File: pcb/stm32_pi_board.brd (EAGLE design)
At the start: 84 x 56 mm, 96 parts, among them IC1 MIC5219-3.3, IC2 ESP-11, IC3 IS31AP2005, IC4 STM32F405RG, IC5 STF203-22, IC6 MIC5219-3.3, IC7 IS31AP2005, IC8 MIC5219-3.3, IC9 UDA1334ATS, Q1 FDG6332C, Q5 BSH205, X1 PJ-043-SMT, X2 DM3AT, X3 XM7D-0512

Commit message: New version of pi_board
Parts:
- removed ESPJ2: LSP10, MyComponents:LSP10
- removed IC1: MIC5219-3.3, MyComponents:SOT23-5
- removed SV2: 75867-331LF, MyComponents:MA03-2
- added C38: 0.1uF, MyComponents:C0805
- added GN-RX-TX: (no value), MyComponents:MA03-1
- added IC10: REG1117, MyComponents:SOT223
- added L3: 1 uH, MyComponents:L0805
- added R26, R27: 330, MyComponents:R0805
- added R28: 1, MyComponents:R0805
- C6: value 470pF -> 100 uF; device MyComponents:C0805 -> MyComponents:CPOL1311
- C7: value 2.2uF -> 47 uF
- D1: value WP154A4SUREQBFZGC -> (none); device MyComponents:RGB-LED-5MM -> MyComponents:RGB-LED-SMD-3X1
- FLASH: value LSP10 -> (none); device MyComponents:LSP10 -> MyComponents:MA02-1
- HSE: device MyComponents:Q-FA-128 -> MyComponents:Q-HC-46X
- moved RESET 63.1 mm to (19.0, 30.8), turned to 90 degrees
- moved C16 62.4 mm to (22.5, 33.2), flipped to the bottom, turned to 0 degrees
- moved SV1 61.5 mm to (11.0, 27.0)
- moved D1 41.8 mm to (82.5, 43.5)
- moved R6 40.3 mm to (78.2, 44.2), flipped to the top, turned to 180 degrees
- moved C6 7.85 mm to (27.0, 29.5), flipped to the top, turned to 270 degrees
- moved R3 7.04 mm to (9.00, 40.0), turned to 180 degrees
- moved C15 6.82 mm to (49.0, 41.8), turned to 270 degrees
- moved C14 5.87 mm to (32.2, 28.8), turned to 90 degrees
- moved C2 5.35 mm to (9.00, 42.5)
- moved IC6 5.13 mm to (13.2, 41.2), turned to 0 degrees
- moved R8 4.76 mm to (56.2, 26.6), flipped to the bottom, turned to 180 degrees
- moved R7 4.65 mm to (50.5, 33.8), turned to 0 degrees
- moved C7 4.14 mm to (30.0, 28.8), flipped to the top, turned to 270 degrees
- moved C3 4.12 mm to (13.2, 45.0)
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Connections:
- removed net D1_BLUE: D1.AB, IC4.10
- removed net D1_GREEN: D1.AG, IC4.9
- removed net D1_RED: D1.AR, IC4.11
- new net N$75: D1.P$1, R27.1
- new net N$85: IC10.2, R28.2
- new net N$90: L3.1, R28.1
- new net PC1: IC4.9, SV3.6
- new net PC2: IC4.10, SV3.5
- new net PC3: IC4.11, SV3.4
- net ESP-IO0: now also FLASH.1; no longer FLASH.MP
- net ESP-RXI: now also GN-RX-TX.2; no longer SV2.5
- net ESP-TXI: now also GN-RX-TX.3; no longer SV2.3
- net GND: now also C38.2, C6.2-, D1.P$2, FLASH.2, GN-RX-TX.1, IC10.1; no longer C6.1, ESPJ2.MP, IC1.2, R6.2, SV2.1
- net N$40: now also D1.P$4, R26.1; no longer D1.C, R6.1
- net N$5: now also D1.P$3, R6.1; no longer C6.2, IC1.4
- net N$78: now also HSE.2; no longer HSE.3
- net PB4: now also R27.2; no longer SV3.11
- net PB5: now also R26.2; no longer SV3.10
- net PB6: now also SV3.11; no longer SV3.9
- net PB7: now also SV3.10; no longer SV3.8
- net PB8: now also R6.2; no longer SV3.7
- net PB9: now also SV3.9; no longer SV3.6
- net PC0: now also SV3.7; no longer SV3.4
- net PC13: now also SV3.8; no longer SV3.5
- net VDD: now also C6.1+, L3.2; no longer IC1.5
- net VIN: now also C38.1, IC10.3; no longer IC1.1, IC1.3
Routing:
- net VDD: track 146.9 -> 118.7 mm, vias 6 -> 8
- net SWCLK: track 22.2 -> 50.0 mm, vias 0 -> 2
- net PC1: track 0.00 -> 25.6 mm
- net PC2: track 0.00 -> 24.8 mm
- net PC3: track 0.00 -> 23.9 mm
- net D1_GREEN: track 18.9 -> 0.00 mm
- net D1_BLUE: track 17.0 -> 0.00 mm
- net ESP-IO0: track 38.3 -> 22.4 mm
- net SWDIO: track 36.6 -> 50.5 mm, vias 0 -> 2
- net D1_RED: track 13.7 -> 0.00 mm
- net ESP-TXI: track 25.8 -> 13.8 mm
- net PC13: track 38.1 -> 26.9 mm
- net GND: track 101.3 -> 90.6 mm, vias 19 -> 21
- net ESP-ON1: track 45.0 -> 36.2 mm
- net ESP-RXI: track 23.3 -> 14.5 mm
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- added copper zone on layer 1, net VDD
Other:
- board text added: "PC1"
- board text added: "PC2"
- board text added: "PC3"
- board text added: "VCC/"
- board text added: "x3"
- board text removed: "PB4"
- board text removed: "PB5"
- board text removed: "PB8"
- board text removed: "RX"
- board text removed: "TX"
- board text removed: "VCC"

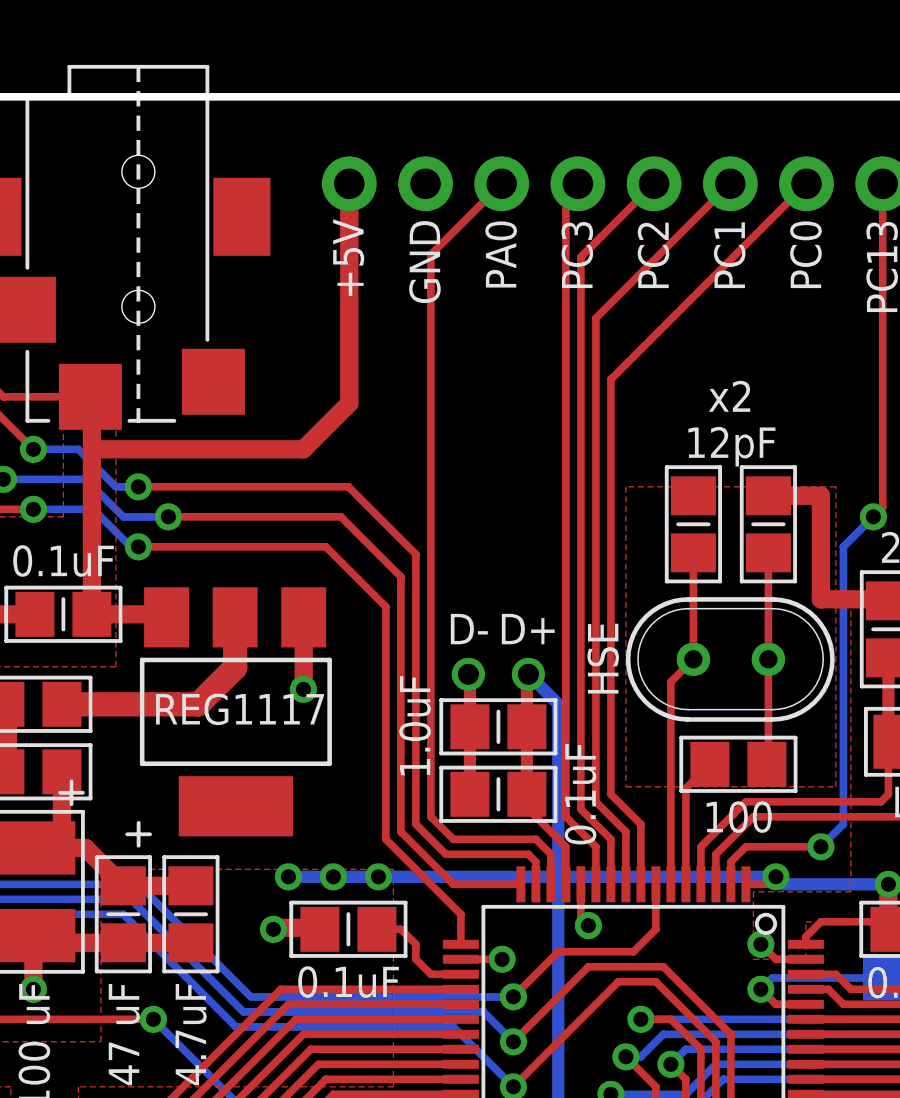
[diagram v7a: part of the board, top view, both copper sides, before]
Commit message: Added LMT86
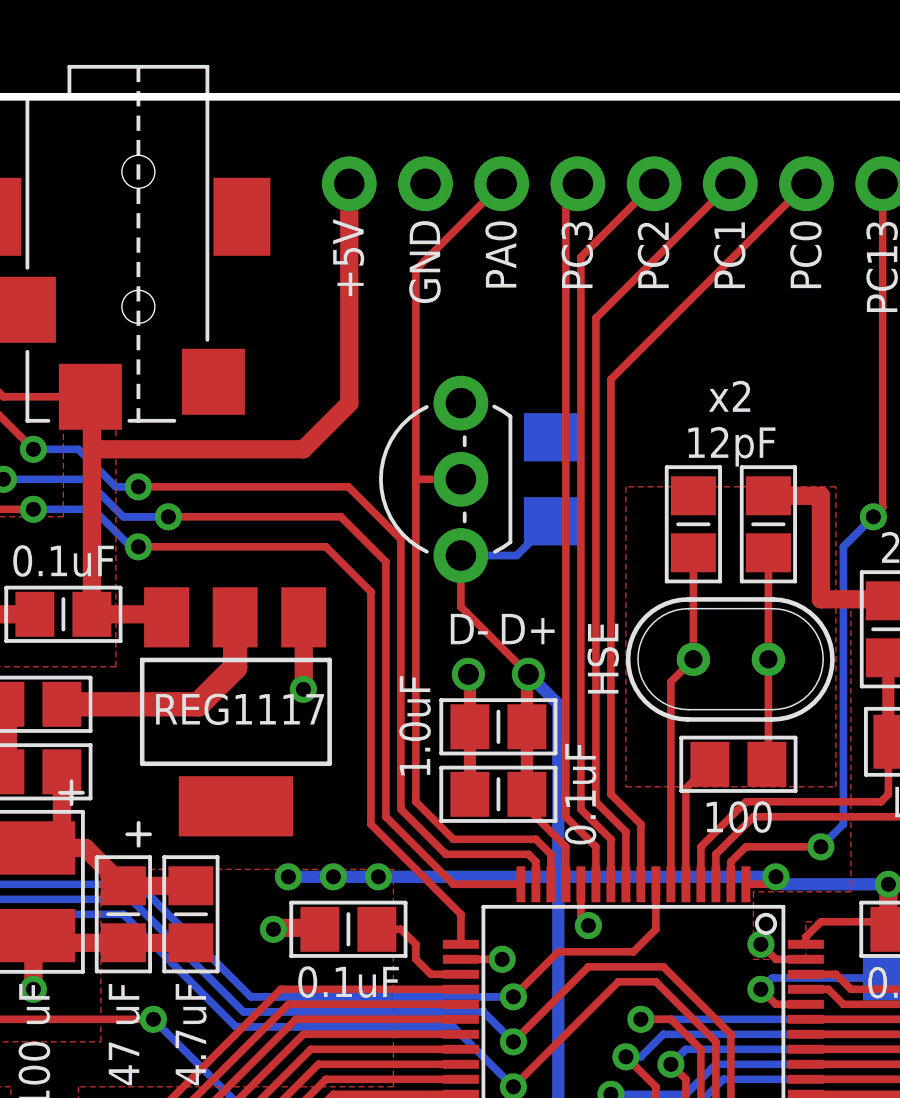
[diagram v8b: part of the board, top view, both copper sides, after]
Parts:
- added C39: 0.1 uF, rcl:C1206
- added IC1: LMT86, MyComponents:LMT86
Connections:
- net GND: now also C39.1, IC1.GND
- net PA0: now also IC1.OUT
- net VDD: now also C39.2, IC1.VDD
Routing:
- net VDD: track 118.7 -> 127.1 mm
- net PA0: track 27.6 -> 29.5 mm
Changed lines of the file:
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@@
 <layer number="21" name="tPlace" color="7" fill="1" visible="yes" active="yes"/>
 <layer number="22" name="bPlace" color="7" fill="1" visible="yes" active="yes"/>
-<layer number="23" name="tOrigins" color="15" fill="1" visible="no" active="yes"/>
+<layer number="23" name="tOrigins" color="15" fill="1" visible="yes" active="yes"/>
 <layer number="24" name="bOrigins" color="15" fill="1" visible="yes" active="yes"/>
-<layer number="25" name="tNames" color="7" fill="1" visible="no" active="yes"/>
+<layer number="25" name="tNames" color="7" fill="1" visible="yes" active="yes"/>
 <layer number="26" name="bNames" color="7" fill="1" visible="yes" active="yes"/>
-<layer number="27" name="tValues" color="7" fill="1" visible="no" active="yes"/>
-<layer number="28" name="bValues" color="7" fill="1" visible="no" active="yes"/>
+<layer number="27" name="tValues" color="7" fill="1" visible="yes" active="yes"/>
+<layer number="28" name="bValues" color="7" fill="1" visible="yes" active="yes"/>
 <layer number="29" name="tStop" color="7" fill="3" visible="no" active="yes"/>
 <layer number="30" name="bStop" color="7" fill="6" visible="no" active="yes"/>
@@
 <attribute name="VALUE" x="24.75" y="35.73" size="1.016" layer="25" rot="R180" align="center-left"/>
 </element>
+<element name="IC1" library="MyComponents" package="LMT86" value="LMT86" x="41.25" y="43.25" locked="yes" smashed="yes" rot="R90">
+<attribute name="VALUE" x="43.25" y="43.25" size="1.016" layer="27" ratio="10" rot="R270" align="bottom-center"/>
+</element>
+<element name="C39" library="rcl" package="C1206" value="0.1 uF" x="44.25" y="43.25" locked="yes" smashed="yes" rot="MR270">
+<attribute name="VALUE" x="45.774" y="43.25" size="1.016" layer="26" rot="MR90" align="bottom-center"/>
+</element>
 </elements>
 <signals>
@@
 <wire x1="36.0106" y1="36.2606" x2="36" y2="36.25" width="0.6096" layer="1"/>
 <wire x1="27" y1="28.038" x2="27" y2="26.25" width="0.6096" layer="1"/>
+<contactref element="IC1" pad="GND"/>
+<contactref element="C39" pad="1"/>
 </signal>
 <signal name="VIN">
@@
 <wire x1="44.75" y1="31" x2="43.45" y2="32.3" width="0.254" layer="1"/>
 <wire x1="43.45" y1="32.3" x2="43.45" y2="32.75" width="0.254" layer="1"/>
+<contactref element="IC1" pad="VDD"/>
+<contactref element="C39" pad="2"/>
+<wire x1="41.25" y1="40.71" x2="41.25" y2="39" width="0.254" layer="1"/>
+<wire x1="41.25" y1="39" x2="43.5" y2="36.75" width="0.254" layer="1"/>
+<wire x1="41.25" y1="40.71" x2="43.11" y2="40.71" width="0.254" layer="16"/>
+<wire x1="43.11" y1="40.71" x2="44.25" y2="41.85" width="0.254" layer="16"/>
 </signal>
 <signal name="NRST">
@@
 <wire x1="43.75" y1="31.25" x2="41" y2="31.25" width="0.254" layer="1"/>
 <contactref element="SV3" pad="3"/>
-<wire x1="40.25" y1="50.74" x2="42.61" y2="53.1" width="0.254" layer="1"/>
-<wire x1="41" y1="31.25" x2="40.25" y2="32" width="0.254" layer="1"/>
-<wire x1="40.25" y1="32" x2="40.25" y2="50.74" width="0.254" layer="1"/>
+<wire x1="39.75" y1="50.24" x2="42.61" y2="53.1" width="0.254" layer="1"/>
+<wire x1="41" y1="31.25" x2="39.75" y2="32.5" width="0.254" layer="1"/>
+<wire x1="39.75" y1="32.5" x2="39.75" y2="43.25" width="0.254" layer="1"/>
+<contactref element="IC1" pad="OUT"/>
+<wire x1="39.75" y1="43.25" x2="39.75" y2="50.24" width="0.254" layer="1"/>
+<wire x1="41.25" y1="43.25" x2="39.75" y2="43.25" width="0.254" layer="1"/>
 </signal>
 <signal name="ESP-TX">
@@
 <wire x1="43.25" y1="29.75" x2="41" y2="29.75" width="0.254" layer="1"/>
 <wire x1="23.5" y1="45.75" x2="26" y2="43.25" width="0.254" layer="1"/>
-<wire x1="39.25" y1="40" x2="39.25" y2="31.5" width="0.254" layer="1"/>
-<wire x1="41" y1="29.75" x2="39.25" y2="31.5" width="0.254" layer="1"/>
+<wire x1="38.75" y1="40.5" x2="38.75" y2="32" width="0.254" layer="1"/>
+<wire x1="41" y1="29.75" x2="38.75" y2="32" width="0.254" layer="1"/>
 <wire x1="31.5" y1="42" x2="37.25" y2="42" width="0.254" layer="1"/>
-<wire x1="37.25" y1="42" x2="39.25" y2="40" width="0.254" layer="1"/>
+<wire x1="37.25" y1="42" x2="38.75" y2="40.5" width="0.254" layer="1"/>
 <wire x1="23.1" y1="45.75" x2="23.5" y2="45.75" width="0.254" layer="1"/>
 <wire x1="31.5" y1="42" x2="30" y2="42" width="0.254" layer="16"/>
@@
 <wire x1="41.25" y1="27.75" x2="41.25" y2="28.75" width="0.254" layer="1"/>
 <wire x1="23.1" y1="43.25" x2="24.75" y2="43.25" width="0.254" layer="1"/>
-<wire x1="41.25" y1="28.75" x2="38.75" y2="31.25" width="0.254" layer="1"/>
-<wire x1="38.75" y1="31.25" x2="38.75" y2="39" width="0.254" layer="1"/>
-<wire x1="36.75" y1="41" x2="38.75" y2="39" width="0.254" layer="1"/>
+<wire x1="41.25" y1="28.75" x2="38.25" y2="31.75" width="0.254" layer="1"/>
+<wire x1="38.25" y1="31.75" x2="38.25" y2="39.5" width="0.254" layer="1"/>
+<wire x1="36.75" y1="41" x2="38.25" y2="39.5" width="0.254" layer="1"/>
 <wire x1="27" y1="42.25" x2="25.75" y2="42.25" width="0.254" layer="1"/>
 <wire x1="25.75" y1="42.25" x2="24.75" y2="43.25" width="0.254" layer="1"/>
@@
 <wire x1="19.75" y1="48.75" x2="19.75" y2="50.5" width="0.254" layer="1"/>
 <wire x1="19.75" y1="50.5" x2="18" y2="52.25" width="0.254" layer="1"/>
-<wire x1="39.75" y1="40.75" x2="39.75" y2="31.75" width="0.254" layer="1"/>
-<wire x1="39.75" y1="31.75" x2="40.75" y2="30.75" width="0.254" layer="1"/>
+<wire x1="39.25" y1="41.25" x2="39.25" y2="32.25" width="0.254" layer="1"/>
+<wire x1="39.25" y1="32.25" x2="40.75" y2="30.75" width="0.254" layer="1"/>
 <wire x1="30.5" y1="43" x2="37.5" y2="43" width="0.254" layer="1"/>
-<wire x1="37.5" y1="43" x2="39.75" y2="40.75" width="0.254" layer="1"/>
+<wire x1="37.5" y1="43" x2="39.25" y2="41.25" width="0.254" layer="1"/>
 <wire x1="24" y1="47.25" x2="27" y2="44.25" width="0.254" layer="1"/>
 <wire x1="30.5" y1="43" x2="29.75" y2="43" width="0.254" layer="16"/>
